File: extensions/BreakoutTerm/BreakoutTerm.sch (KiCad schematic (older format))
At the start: 7 parts, among them M1 MH_3.2mm, M2 MH_3.2mm, P1 *, P2 CONN_01X10, P3 *

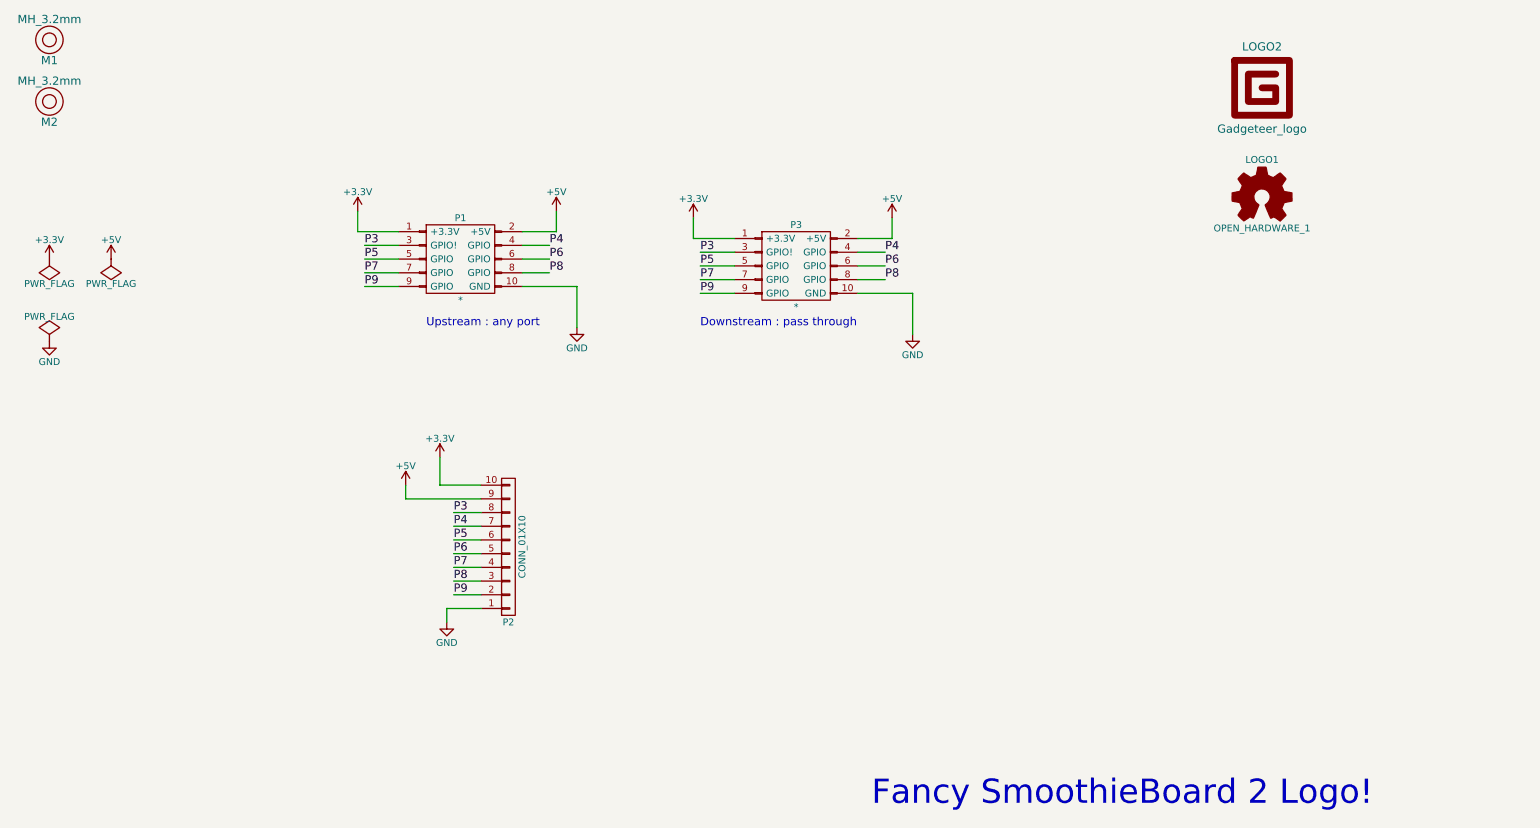
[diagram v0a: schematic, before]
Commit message: Corrected part number for gadgeteer connectors; update libraries; add some doc files
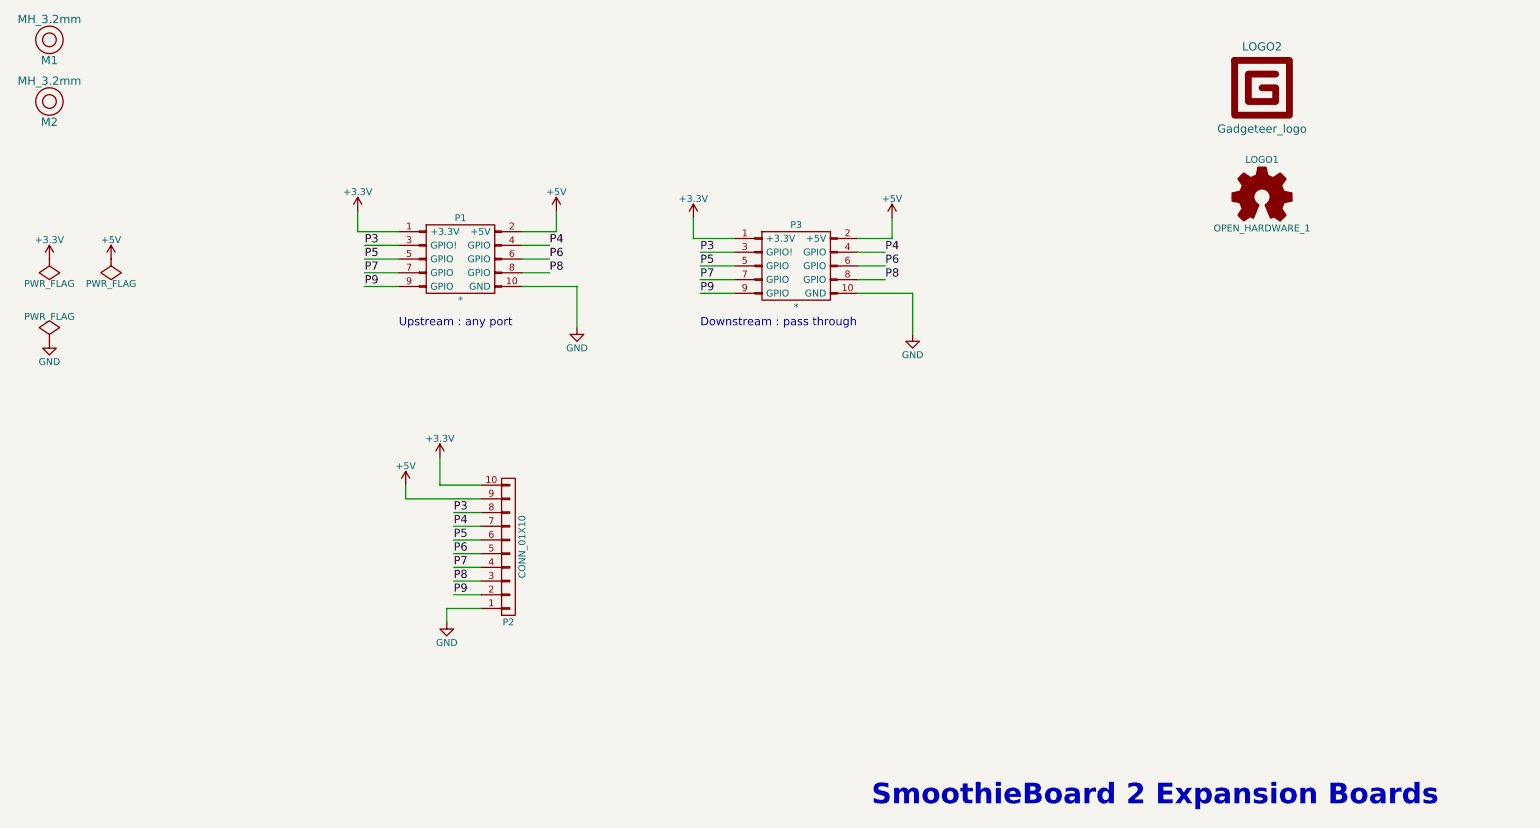
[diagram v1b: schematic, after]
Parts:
- P1: footprint SBV2_Footprints:ESHF-105-01-L-D-SM -> SBV2_Footprints:SHF-105-01-L-D-SM; DKPN SAM8765-ND -> 609-4054-ND; MANF Samtec -> (none); MFPN ESHF-105-01-L-D-SM -> SHF-105-01-L-D-SM
- P3: footprint SBV2_Footprints:ESHF-105-01-L-D-SM -> SBV2_Footprints:SHF-105-01-L-D-SM; DKPN SAM8765-ND -> 609-4054-ND; MFPN ESHF-105-01-L-D-SM -> SHF-105-01-L-D-SM
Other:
- note added: "SmoothieBoard 2 Expansion Boards"
- note removed: "Fancy SmoothieBoard 2 Logo!"
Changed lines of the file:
@@
 Comment4 ""
 $EndDescr
-Text Notes 7100 6900 0    177  ~ 0
-Fancy SmoothieBoard 2 Logo!
-$Comp
-L +3.3V #PWR01
+Text Notes 7100 6900 0    150  ~ 30
+SmoothieBoard 2 Expansion Boards
+$Comp
+L +3.3V #PWR1
 U 1 1 573E07CC
 P 3350 2550
-F 0 "#PWR01" H 3350 2400 50  0001 C CNN
+F 0 "#PWR1" H 3350 2400 50  0001 C CNN
 F 1 "+3.3V" H 3350 2690 50  0000 C CNN
 F 2 "" H 3350 2550 50  0000 C CNN
@@
 $EndComp
 $Comp
-L +5V #PWR02
+L +5V #PWR2
 U 1 1 573E07F5
 P 4800 2550
-F 0 "#PWR02" H 4800 2400 50  0001 C CNN
+F 0 "#PWR2" H 4800 2400 50  0001 C CNN
 F 1 "+5V" H 4800 2690 50  0000 C CNN
 F 2 "" H 4800 2550 50  0000 C CNN
@@
 $EndComp
 $Comp
-L GND #PWR03
+L GND #PWR7
 U 1 1 573E081E
 P 4950 3400
-F 0 "#PWR03" H 4950 3150 50  0001 C CNN
+F 0 "#PWR7" H 4950 3150 50  0001 C CNN
 F 1 "GND" H 4950 3250 50  0000 C CNN
 F 2 "" H 4950 3400 50  0000 C CNN
@@
 	4050 5350 4250 5350
 $Comp
-L GND #PWR04
+L GND #PWR12
 U 1 1 573E0983
 P 4000 5550
-F 0 "#PWR04" H 4000 5300 50  0001 C CNN
+F 0 "#PWR12" H 4000 5300 50  0001 C CNN
 F 1 "GND" H 4000 5400 50  0000 C CNN
 F 2 "" H 4000 5550 50  0000 C CNN
@@
 	4000 5450 4000 5550
 $Comp
-L +3.3V #PWR05
+L +3.3V #PWR10
 U 1 1 573E09AF
 P 3950 4350
-F 0 "#PWR05" H 3950 4200 50  0001 C CNN
+F 0 "#PWR10" H 3950 4200 50  0001 C CNN
 F 1 "+3.3V" H 3950 4490 50  0000 C CNN
 F 2 "" H 3950 4350 50  0000 C CNN
@@
 $EndComp
 $Comp
-L +5V #PWR06
+L +5V #PWR11
 U 1 1 573E09C3
 P 3700 4550
-F 0 "#PWR06" H 3700 4400 50  0001 C CNN
+F 0 "#PWR11" H 3700 4400 50  0001 C CNN
 F 1 "+5V" H 3700 4690 50  0000 C CNN
 F 2 "" H 3700 4550 50  0000 C CNN
@@
 	4750 3000 4550 3000
 $Comp
-L +3.3V #PWR07
+L +3.3V #PWR3
 U 1 1 573E0BA7
 P 5800 2600
-F 0 "#PWR07" H 5800 2450 50  0001 C CNN
+F 0 "#PWR3" H 5800 2450 50  0001 C CNN
 F 1 "+3.3V" H 5800 2740 50  0000 C CNN
 F 2 "" H 5800 2600 50  0000 C CNN
@@
 $EndComp
 $Comp
-L +5V #PWR08
+L +5V #PWR4
 U 1 1 573E0BAD
 P 7250 2600
-F 0 "#PWR08" H 7250 2450 50  0001 C CNN
+F 0 "#PWR4" H 7250 2450 50  0001 C CNN
 F 1 "+5V" H 7250 2740 50  0000 C CNN
 F 2 "" H 7250 2600 50  0000 C CNN
@@
 $EndComp
 $Comp
-L GND #PWR09
+L GND #PWR8
 U 1 1 573E0BB3
 P 7400 3450
-F 0 "#PWR09" H 7400 3200 50  0001 C CNN
+F 0 "#PWR8" H 7400 3200 50  0001 C CNN
 F 1 "GND" H 7400 3300 50  0000 C CNN
 F 2 "" H 7400 3450 50  0000 C CNN
@@
 $EndComp
 $Comp
-L +3.3V #PWR010
+L +3.3V #PWR5
 U 1 1 573E0C24
 P 1100 2900
-F 0 "#PWR010" H 1100 2750 50  0001 C CNN
+F 0 "#PWR5" H 1100 2750 50  0001 C CNN
 F 1 "+3.3V" H 1100 3040 50  0000 C CNN
 F 2 "" H 1100 2900 50  0000 C CNN
@@
 $EndComp
 $Comp
-L +5V #PWR011
+L +5V #PWR6
 U 1 1 573E0C38
 P 1550 2900
-F 0 "#PWR011" H 1550 2750 50  0001 C CNN
+F 0 "#PWR6" H 1550 2750 50  0001 C CNN
 F 1 "+5V" H 1550 3040 50  0000 C CNN
 F 2 "" H 1550 2900 50  0000 C CNN
@@
 $EndComp
 $Comp
-L GND #PWR012
+L GND #PWR9
 U 1 1 573E0C4C
 P 1100 3500
-F 0 "#PWR012" H 1100 3250 50  0001 C CNN
+F 0 "#PWR9" H 1100 3250 50  0001 C CNN
 F 1 "GND" H 1100 3350 50  0000 C CNN
 F 2 "" H 1100 3500 50  0000 C CNN
@@
 $EndComp
 $Comp
-L PWR_FLAG #FLG013
+L PWR_FLAG #FLG3
 U 1 1 573E0C63
 P 1100 3500
-F 0 "#FLG013" H 1100 3595 50  0001 C CNN
+F 0 "#FLG3" H 1100 3595 50  0001 C CNN
 F 1 "PWR_FLAG" H 1100 3680 50  0000 C CNN
 F 2 "" H 1100 3500 50  0000 C CNN
@@
 $EndComp
 $Comp
-L PWR_FLAG #FLG014
+L PWR_FLAG #FLG1
 U 1 1 573E0C7E
 P 1100 2900
-F 0 "#FLG014" H 1100 2995 50  0001 C CNN
+F 0 "#FLG1" H 1100 2995 50  0001 C CNN
 F 1 "PWR_FLAG" H 1100 3080 50  0000 C CNN
 F 2 "" H 1100 2900 50  0000 C CNN
@@
 $EndComp
 $Comp
-L PWR_FLAG #FLG015
+L PWR_FLAG #FLG2
 U 1 1 573E0CE7
 P 1550 2900
-F 0 "#FLG015" H 1550 2995 50  0001 C CNN
+F 0 "#FLG2" H 1550 2995 50  0001 C CNN
 F 1 "PWR_FLAG" H 1550 3080 50  0000 C CNN
 F 2 "" H 1550 2900 50  0000 C CNN
@@
 	1    0    0    -1
 $EndComp
+Text Notes 3650 3400 0    60   ~ 0
+Upstream : any port
+Text Notes 5850 3400 0    60   ~ 0
+Downstream : pass through
 $Comp
 L Conn-Y P1
-U 1 1 573F3F4E
+U 1 1 5749CDEF
 P 4100 2900
 F 0 "P1" H 4100 3200 50  0000 C CNN
 F 1 "*" H 4100 2600 50  0000 C CNN
-F 2 "SBV2_Footprints:ESHF-105-01-L-D-SM" H 4150 2450 50  0001 C CNN
+F 2 "SBV2_Footprints:SHF-105-01-L-D-SM" H 4150 2450 50  0001 C CNN
 F 3 "" H 4100 1700 50  0000 C CNN
-F 4 "ESHF-105-01-L-D-SM " H 4100 2250 50  0001 C CNN "MFPN"
-F 5 "SAM8765-ND " H 4150 2350 50  0001 C CNN "DKPN"
-F 6 "Samtec" H 4100 2900 60  0001 C CNN "MANF"
+F 4 "SHF-105-01-L-D-SM" H 4100 2250 50  0001 C CNN "MFPN"
+F 5 "609-4054-ND" H 4150 2350 50  0001 C CNN "DKPN"
 	1    4100 2900
 	1    0    0    -1
@@
 $Comp
 L Conn-Y P3
-U 1 1 573F3FDE
+U 1 1 5749CF64
 P 6550 2950
 F 0 "P3" H 6550 3250 50  0000 C CNN
 F 1 "*" H 6550 2650 50  0000 C CNN
-F 2 "SBV2_Footprints:ESHF-105-01-L-D-SM" H 6600 2500 50  0001 C CNN
+F 2 "SBV2_Footprints:SHF-105-01-L-D-SM" H 6600 2500 50  0001 C CNN
 F 3 "" H 6550 1750 50  0000 C CNN
-F 4 "ESHF-105-01-L-D-SM " H 6550 2300 50  0001 C CNN "MFPN"
-F 5 "SAM8765-ND " H 6600 2400 50  0001 C CNN "DKPN"
+F 4 "SHF-105-01-L-D-SM" H 6550 2300 50  0001 C CNN "MFPN"
+F 5 "609-4054-ND" H 6600 2400 50  0001 C CNN "DKPN"
 	1    6550 2950
 	1    0    0    -1
 $EndComp
-Text Notes 3850 3400 0    60   ~ 0
-Upstream : any port
-Text Notes 5850 3400 0    60   ~ 0
-Downstream : pass through
 $EndSCHEMATC
